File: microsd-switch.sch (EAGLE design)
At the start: 8 parts, among them IC1 74LS157D, IC2 74LS157D, U1 USD-SOCKETNEW, U2 MICRO-SDCARD-PCB, U3 MICRO-SDCARD-TARGET

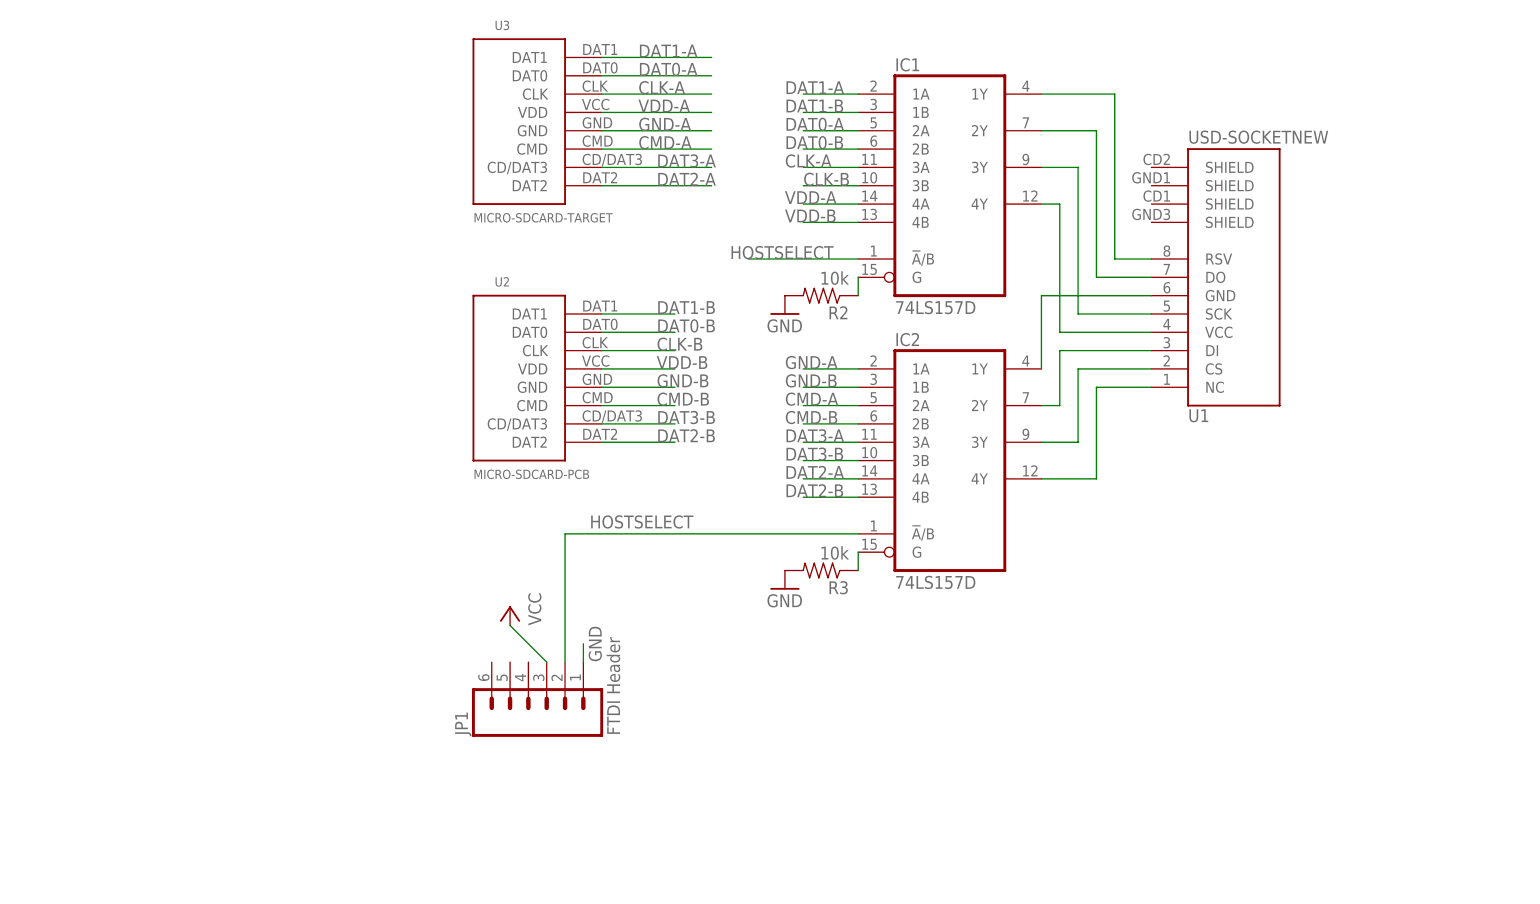
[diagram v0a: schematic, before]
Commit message: Update microsd-switcher project files
Added pics, redesigned board, added a "legs" board.

Signed-off-by: Joel Fernandes <joelf@ti.com>
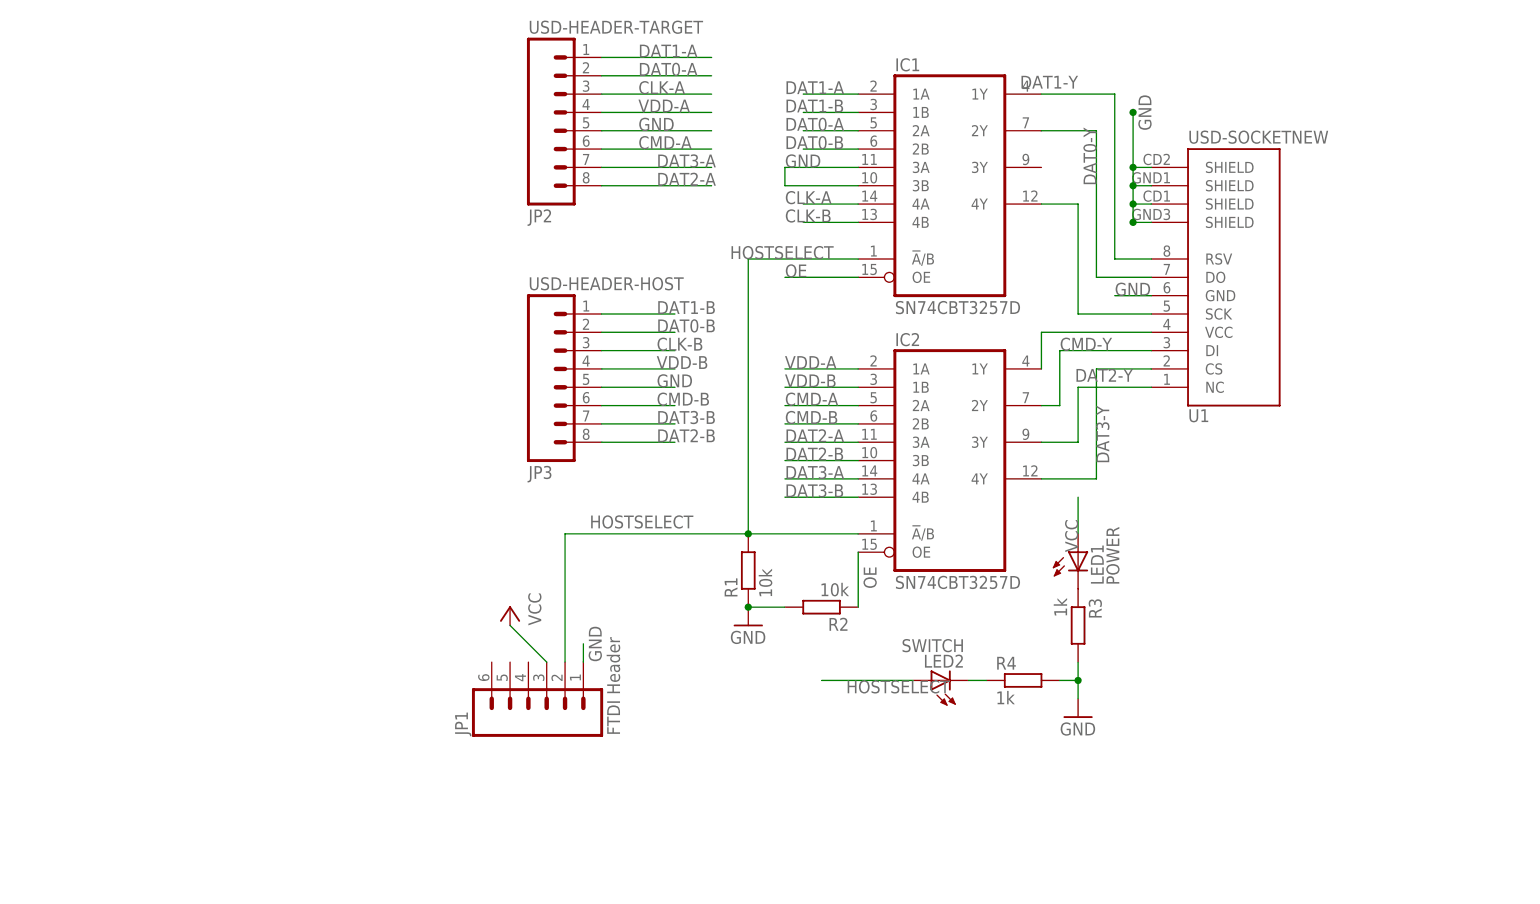
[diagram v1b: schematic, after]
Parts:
- removed U2: MICRO-SDCARD-PCB, SparkFun:MICRO-SDCARDUSDPCB
- removed U3: MICRO-SDCARD-TARGET, SparkFun:MICRO-SDCARDUSDPCB
- added JP2: USD-HEADER-TARGET, SparkFun:M08LOCK
- added JP3: USD-HEADER-HOST, SparkFun:M08LOCK
- added LED1: POWER, led:LEDCHIP-LED0805
- added LED2: SWITCH, led:LEDCHIP-LED0805
- added R1: 10k, rcl:R-EU_R1206
- added R4: 1k, rcl:R-EU_R1206
- IC1, IC2: value 74LS157D -> SN74CBT3257D; device 74xx-eu:74LS157D -> joels-parts:SN74CBT3257D
- R2: device SparkFun:RESISTORPTH-1/4W -> rcl:R-EU_R1206
- R3: value 10k -> 1k; device SparkFun:RESISTORPTH-1/4W -> rcl:R-EU_R1206
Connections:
- net N$1 renamed DAT1-Y
- net N$2 renamed DAT0-Y
- net N$6 renamed CMD-Y
- removed net GND-A: IC2A.1A, U3.GND
- removed net GND-B: IC2A.1B, U2.GND
- removed net N$18: IC2A.G, R3.1
- removed net N$5: IC1A.4Y, U1.VCC
- removed net N$7: IC2A.3Y, U1.CS
- removed net N$8: IC2A.4Y, U1.NC
- removed net N$9: IC1A.G, R2.1
- new net DAT2-Y: IC2A.3Y, U1.NC
- new net DAT3-Y: IC2A.4Y, U1.CS
- new net N$1: IC1A.4Y, U1.SCK
- new net N$2: IC2A.1Y, U1.VCC
- new net OE: IC1A.OE, IC2A.OE, R2.1
- net CLK-A: now also IC1A.4A, JP2.3; no longer IC1A.3A, U3.CLK
- net CLK-B: now also IC1A.4B, JP3.3; no longer IC1A.3B, U2.CLK
- net CMD-A: now also JP2.6; no longer U3.CMD
- net CMD-B: now also JP3.6; no longer U2.CMD
- net DAT0-A: now also JP2.2; no longer U3.DAT0
- net DAT0-B: now also JP3.2; no longer U2.DAT0
- net DAT1-A: now also JP2.1; no longer U3.DAT1
- net DAT1-B: now also JP3.1; no longer U2.DAT1
- net DAT2-A: now also IC2A.3A, JP2.8; no longer IC2A.4A, U3.DAT2
- net DAT2-B: now also IC2A.3B, JP3.8; no longer IC2A.4B, U2.DAT2
- net DAT3-A: now also IC2A.4A, JP2.7; no longer IC2A.3A, U3.CD/DAT3
- net DAT3-B: now also IC2A.4B, JP3.7; no longer IC2A.3B, U2.CD/DAT3
- net GND: now also IC1A.3A, IC1A.3B, JP2.5, JP3.5, R1.1, R4.2, U1.GND, U1.SHIELD@1, U1.SHIELD@2, U1.SHIELD@3, U1.SHIELD@4
- net HOSTSELECT: now also LED2.A, R1.2
- net N$3: now also LED1.C, R3.1; no longer IC2A.1Y, U1.GND
- net N$4: now also LED2.C, R4.1; no longer IC1A.3Y, U1.SCK
- net VCC: now also LED1.A
- net VDD-A: now also IC2A.1A, JP2.4; no longer IC1A.4A, U3.VDD
- net VDD-B: now also IC2A.1B, JP3.4; no longer IC1A.4B, U2.VDD

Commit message: Update license
Signed-off-by: Joel Fernandes <joelf@ti.com>
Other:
- note added: "(C) Joel Fernandes"
- note added: "License CC-BY-NC-SA 3.0"
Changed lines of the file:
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@@
 <sheet>
 <plain>
+<text x="76.2" y="17.78" size="2.1844" layer="91">License CC-BY-NC-SA 3.0</text>
+<text x="76.2" y="12.7" size="2.1844" layer="91">(C) Joel Fernandes</text>
 </plain>
 <instances>

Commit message: MicroSD Switch Rev Alpha released
Signed-off-by: Joel Fernandes <joelf@ti.com>
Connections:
- net N$1 renamed CLK-Y
- net CLK-A: now also JP2.4; no longer JP2.3
- net CLK-B: now also JP3.4; no longer JP3.3
- net GND: now also JP2.3, JP3.3; no longer JP2.5, JP3.5
- net VDD-A: now also JP2.5; no longer JP2.4
- net VDD-B: now also JP3.5; no longer JP3.4
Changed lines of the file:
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@@
 <layer number="18" name="Vias" color="2" fill="1" visible="no" active="no"/>
 <layer number="19" name="Unrouted" color="6" fill="1" visible="no" active="no"/>
-<layer number="20" name="Dimension" color="7" fill="1" visible="no" active="no"/>
-<layer number="21" name="tPlace" color="16" fill="1" visible="no" active="no"/>
-<layer number="22" name="bPlace" color="14" fill="1" visible="no" active="no"/>
+<layer number="20" name="Dimension" color="15" fill="1" visible="no" active="no"/>
+<layer number="21" name="tPlace" color="7" fill="1" visible="no" active="no"/>
+<layer number="22" name="bPlace" color="7" fill="1" visible="no" active="no"/>
 <layer number="23" name="tOrigins" color="15" fill="1" visible="no" active="no"/>
 <layer number="24" name="bOrigins" color="15" fill="1" visible="no" active="no"/>
@@
 <layer number="29" name="tStop" color="7" fill="3" visible="no" active="no"/>
 <layer number="30" name="bStop" color="7" fill="6" visible="no" active="no"/>
-<layer number="31" name="tCream" color="11" fill="4" visible="no" active="no"/>
+<layer number="31" name="tCream" color="7" fill="4" visible="no" active="no"/>
 <layer number="32" name="bCream" color="7" fill="5" visible="no" active="no"/>
 <layer number="33" name="tFinish" color="6" fill="3" visible="no" active="no"/>
@@
 <layer number="47" name="Measures" color="7" fill="1" visible="no" active="no"/>
 <layer number="48" name="Document" color="7" fill="1" visible="no" active="no"/>
-<layer number="49" name="Reference" color="13" fill="1" visible="no" active="no"/>
+<layer number="49" name="Reference" color="7" fill="1" visible="no" active="no"/>
 <layer number="50" name="dxf" color="7" fill="1" visible="no" active="no"/>
-<layer number="51" name="tDocu" color="14" fill="1" visible="no" active="no"/>
+<layer number="51" name="tDocu" color="7" fill="1" visible="no" active="no"/>
 <layer number="52" name="bDocu" color="7" fill="1" visible="no" active="no"/>
 <layer number="53" name="tGND_GNDA" color="7" fill="9" visible="no" active="no"/>
@@
 </classes>
 <parts>
-<part name="U1" library="SparkFun" deviceset="USD-SOCKET" device="NEW"/>
 <part name="JP1" library="SparkFun" deviceset="M06" device="LOCK" value="FTDI Header"/>
 <part name="GND2" library="supply1" deviceset="GND" device=""/>
@@
 <part name="LED2" library="led" deviceset="LED" device="CHIP-LED0805" value="SWITCH"/>
 <part name="GND1" library="supply1" deviceset="GND" device=""/>
+<part name="U1" library="SparkFun" deviceset="USD-SOCKET" device="NEW"/>
 </parts>
 <sheets>
@@
 </plain>
 <instances>
-<instance part="U1" gate="G$1" x="81.28" y="45.72" rot="MR180"/>
 <instance part="JP1" gate="G$1" x="-10.16" y="-10.16" rot="R90"/>
 <instance part="GND2" gate="1" x="17.78" y="0"/>
@@
 <instance part="LED2" gate="G$1" x="43.18" y="-7.62" rot="R90"/>
 <instance part="GND1" gate="1" x="63.5" y="-12.7"/>
+<instance part="U1" gate="G$1" x="81.28" y="45.72" rot="MR180"/>
 </instances>
 <busses>
@@
 </segment>
 <segment>
-<pinref part="JP2" gate="G$1" pin="4"/>
-<wire x1="-2.54" y1="71.12" x2="12.7" y2="71.12" width="0.1524" layer="91"/>
-<label x="2.54" y="71.12" size="1.778" layer="95"/>
+<pinref part="JP2" gate="G$1" pin="5"/>
+<wire x1="-2.54" y1="68.58" x2="12.7" y2="68.58" width="0.1524" layer="91"/>
+<label x="2.54" y="68.58" size="1.778" layer="95"/>
 </segment>
 </net>
@@
 </segment>
 <segment>
-<pinref part="JP3" gate="G$1" pin="3"/>
-<wire x1="-2.54" y1="38.1" x2="7.62" y2="38.1" width="0.1524" layer="91"/>
-<label x="5.08" y="38.1" size="1.778" layer="95"/>
+<pinref part="JP3" gate="G$1" pin="4"/>
+<wire x1="-2.54" y1="35.56" x2="7.62" y2="35.56" width="0.1524" layer="91"/>
+<label x="5.08" y="35.56" size="1.778" layer="95"/>
 </segment>
 </net>
@@
 </segment>
 <segment>
-<pinref part="JP3" gate="G$1" pin="4"/>
-<wire x1="-2.54" y1="35.56" x2="7.62" y2="35.56" width="0.1524" layer="91"/>
-<label x="5.08" y="35.56" size="1.778" layer="95"/>
+<pinref part="JP3" gate="G$1" pin="5"/>
+<wire x1="-2.54" y1="33.02" x2="7.62" y2="33.02" width="0.1524" layer="91"/>
+<label x="5.08" y="33.02" size="1.778" layer="95"/>
 </segment>
 </net>
@@
 <wire x1="58.42" y1="73.66" x2="68.58" y2="73.66" width="0.1524" layer="91"/>
 <wire x1="68.58" y1="73.66" x2="68.58" y2="50.8" width="0.1524" layer="91"/>
-<pinref part="U1" gate="G$1" pin="RSV"/>
 <wire x1="68.58" y1="50.8" x2="73.66" y2="50.8" width="0.1524" layer="91"/>
 <label x="63.5" y="76.2" size="1.778" layer="95" rot="R180"/>
 <pinref part="IC1" gate="A" pin="1Y"/>
+<pinref part="U1" gate="G$1" pin="RSV"/>
 </segment>
 </net>
@@
 <wire x1="58.42" y1="68.58" x2="66.04" y2="68.58" width="0.1524" layer="91"/>
 <wire x1="66.04" y1="68.58" x2="66.04" y2="48.26" width="0.1524" layer="91"/>
-<pinref part="U1" gate="G$1" pin="DO"/>
 <wire x1="66.04" y1="48.26" x2="73.66" y2="48.26" width="0.1524" layer="91"/>
 <label x="66.04" y="60.96" size="1.778" layer="95" rot="R90"/>
 <pinref part="IC1" gate="A" pin="2Y"/>
+<pinref part="U1" gate="G$1" pin="DO"/>
 </segment>
 </net>
@@
 <wire x1="58.42" y1="30.48" x2="60.96" y2="30.48" width="0.1524" layer="91"/>
 <wire x1="60.96" y1="30.48" x2="60.96" y2="38.1" width="0.1524" layer="91"/>
-<pinref part="U1" gate="G$1" pin="DI"/>
 <wire x1="60.96" y1="38.1" x2="73.66" y2="38.1" width="0.1524" layer="91"/>
 <label x="60.96" y="38.1" size="1.778" layer="95"/>
 <pinref part="IC2" gate="A" pin="2Y"/>
+<pinref part="U1" gate="G$1" pin="DI"/>
 </segment>
 </net>
@@
 </segment>
 <segment>
-<pinref part="U1" gate="G$1" pin="GND"/>
 <wire x1="73.66" y1="45.72" x2="68.58" y2="45.72" width="0.1524" layer="91"/>
 <label x="68.58" y="45.72" size="1.778" layer="95"/>
-</segment>
-<segment>
-<pinref part="U1" gate="G$1" pin="SHIELD@1"/>
+<pinref part="U1" gate="G$1" pin="GND"/>
+</segment>
+<segment>
 <wire x1="73.66" y1="55.88" x2="71.12" y2="55.88" width="0.1524" layer="91"/>
 <wire x1="71.12" y1="55.88" x2="71.12" y2="58.42" width="0.1524" layer="91"/>
 <wire x1="71.12" y1="71.12" x2="71.12" y2="63.5" width="0.1524" layer="91"/>
-<pinref part="U1" gate="G$1" pin="SHIELD@4"/>
 <wire x1="73.66" y1="63.5" x2="71.12" y2="63.5" width="0.1524" layer="91"/>
 <wire x1="71.12" y1="63.5" x2="71.12" y2="60.96" width="0.1524" layer="91"/>
-<pinref part="U1" gate="G$1" pin="SHIELD@3"/>
 <wire x1="73.66" y1="60.96" x2="71.12" y2="60.96" width="0.1524" layer="91"/>
 <wire x1="71.12" y1="60.96" x2="71.12" y2="58.42" width="0.1524" layer="91"/>
-<pinref part="U1" gate="G$1" pin="SHIELD@2"/>
 <wire x1="71.12" y1="58.42" x2="73.66" y2="58.42" width="0.1524" layer="91"/>
 <label x="73.66" y="68.58" size="1.778" layer="95" rot="R90"/>
@@
 <junction x="71.12" y="55.88"/>
 <junction x="71.12" y="71.12"/>
+<pinref part="U1" gate="G$1" pin="SHIELD@3"/>
+<pinref part="U1" gate="G$1" pin="SHIELD@1"/>
+<pinref part="U1" gate="G$1" pin="SHIELD@2"/>
+<pinref part="U1" gate="G$1" pin="SHIELD@4"/>
 </segment>
 <segment>
@@
 <wire x1="33.02" y1="60.96" x2="22.86" y2="60.96" width="0.1524" layer="91"/>
 <wire x1="22.86" y1="60.96" x2="22.86" y2="63.5" width="0.1524" layer="91"/>
-</segment>
-<segment>
-<pinref part="JP3" gate="G$1" pin="5"/>
-<wire x1="-2.54" y1="33.02" x2="7.62" y2="33.02" width="0.1524" layer="91"/>
-<label x="5.08" y="33.02" size="1.778" layer="95"/>
-</segment>
-<segment>
-<pinref part="JP2" gate="G$1" pin="5"/>
-<wire x1="-2.54" y1="68.58" x2="12.7" y2="68.58" width="0.1524" layer="91"/>
-<label x="2.54" y="68.58" size="1.778" layer="95"/>
 </segment>
 <segment>
@@
 <wire x1="60.96" y1="-7.62" x2="63.5" y2="-7.62" width="0.1524" layer="91"/>
 <junction x="63.5" y="-7.62"/>
+</segment>
+<segment>
+<pinref part="JP2" gate="G$1" pin="3"/>
+<wire x1="-2.54" y1="73.66" x2="12.7" y2="73.66" width="0.1524" layer="91"/>
+<label x="2.54" y="73.66" size="1.778" layer="95"/>
+</segment>
+<segment>
+<pinref part="JP3" gate="G$1" pin="3"/>
+<wire x1="-2.54" y1="38.1" x2="7.62" y2="38.1" width="0.1524" layer="91"/>
+<label x="5.08" y="38.1" size="1.778" layer="95"/>
 </segment>
 </net>
@@
 <pinref part="IC2" gate="A" pin="3Y"/>
 <wire x1="63.5" y1="25.4" x2="63.5" y2="33.02" width="0.1524" layer="91"/>
+<wire x1="63.5" y1="33.02" x2="73.66" y2="33.02" width="0.1524" layer="91"/>
 <pinref part="U1" gate="G$1" pin="NC"/>
-<wire x1="63.5" y1="33.02" x2="73.66" y2="33.02" width="0.1524" layer="91"/>
 </segment>
 </net>
@@
 </segment>
 <segment>
-<pinref part="JP2" gate="G$1" pin="3"/>
-<wire x1="-2.54" y1="73.66" x2="12.7" y2="73.66" width="0.1524" layer="91"/>
-<label x="2.54" y="73.66" size="1.778" layer="95"/>
-</segment>
-</net>
-<net name="N$1" class="0">
+<pinref part="JP2" gate="G$1" pin="4"/>
+<wire x1="-2.54" y1="71.12" x2="12.7" y2="71.12" width="0.1524" layer="91"/>
+<label x="2.54" y="71.12" size="1.778" layer="95"/>
+</segment>
+</net>
+<net name="CLK-Y" class="0">
 <segment>
 <pinref part="IC1" gate="A" pin="4Y"/>
 <wire x1="58.42" y1="58.42" x2="63.5" y2="58.42" width="0.1524" layer="91"/>
 <wire x1="63.5" y1="58.42" x2="63.5" y2="43.18" width="0.1524" layer="91"/>
+<wire x1="63.5" y1="43.18" x2="73.66" y2="43.18" width="0.1524" layer="91"/>
 <pinref part="U1" gate="G$1" pin="SCK"/>
-<wire x1="63.5" y1="43.18" x2="73.66" y2="43.18" width="0.1524" layer="91"/>
 </segment>
 </net>
@@
 <pinref part="IC2" gate="A" pin="1Y"/>
 <wire x1="58.42" y1="35.56" x2="58.42" y2="40.64" width="0.1524" layer="91"/>
+<wire x1="58.42" y1="40.64" x2="73.66" y2="40.64" width="0.1524" layer="91"/>
 <pinref part="U1" gate="G$1" pin="VCC"/>
-<wire x1="58.42" y1="40.64" x2="73.66" y2="40.64" width="0.1524" layer="91"/>
 </segment>
 </net>
@@
 <pinref part="IC2" gate="A" pin="4Y"/>
 <wire x1="58.42" y1="20.32" x2="66.04" y2="20.32" width="0.1524" layer="91"/>
+<wire x1="66.04" y1="35.56" x2="73.66" y2="35.56" width="0.1524" layer="91"/>
 <pinref part="U1" gate="G$1" pin="CS"/>
-<wire x1="66.04" y1="35.56" x2="73.66" y2="35.56" width="0.1524" layer="91"/>
-</segment>
-</net>
+</segment>
+</net>

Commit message: Revert "MicroSD Switch Rev Alpha released"
This reverts commit e0d3fcd5b1a8d34c9a3cecba9fd5e98c93932393.
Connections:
- net CLK-Y renamed N$1
- net CLK-A: now also JP2.3; no longer JP2.4
- net CLK-B: now also JP3.3; no longer JP3.4
- net GND: now also JP2.5, JP3.5; no longer JP2.3, JP3.3
- net VDD-A: now also JP2.4; no longer JP2.5
- net VDD-B: now also JP3.4; no longer JP3.5
